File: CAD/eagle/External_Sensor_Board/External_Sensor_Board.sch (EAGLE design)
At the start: 12 parts, among them J1 SFW15R_FFC, U1 MAX31725MTA+, U2 HSCMNNN1.6BAAA3

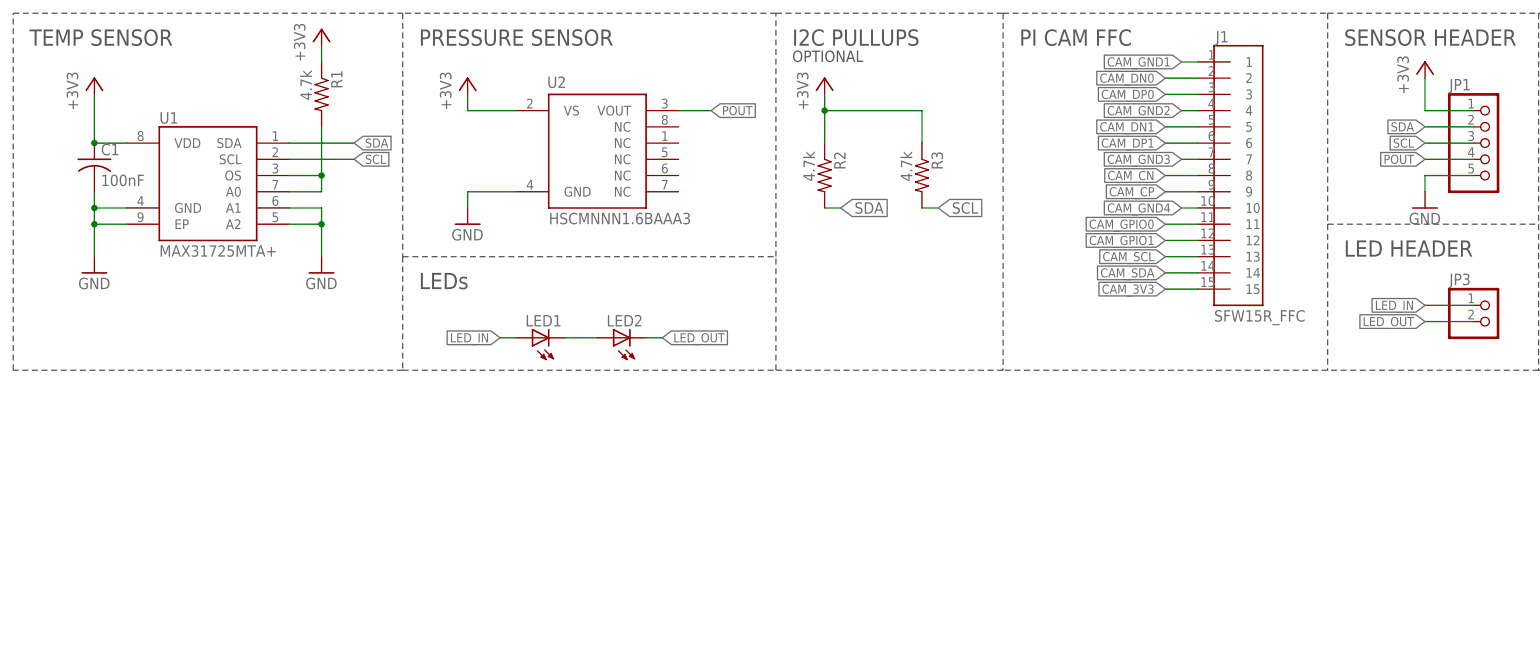
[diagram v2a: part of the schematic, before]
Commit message: Added I2C buffer to external sensor board.
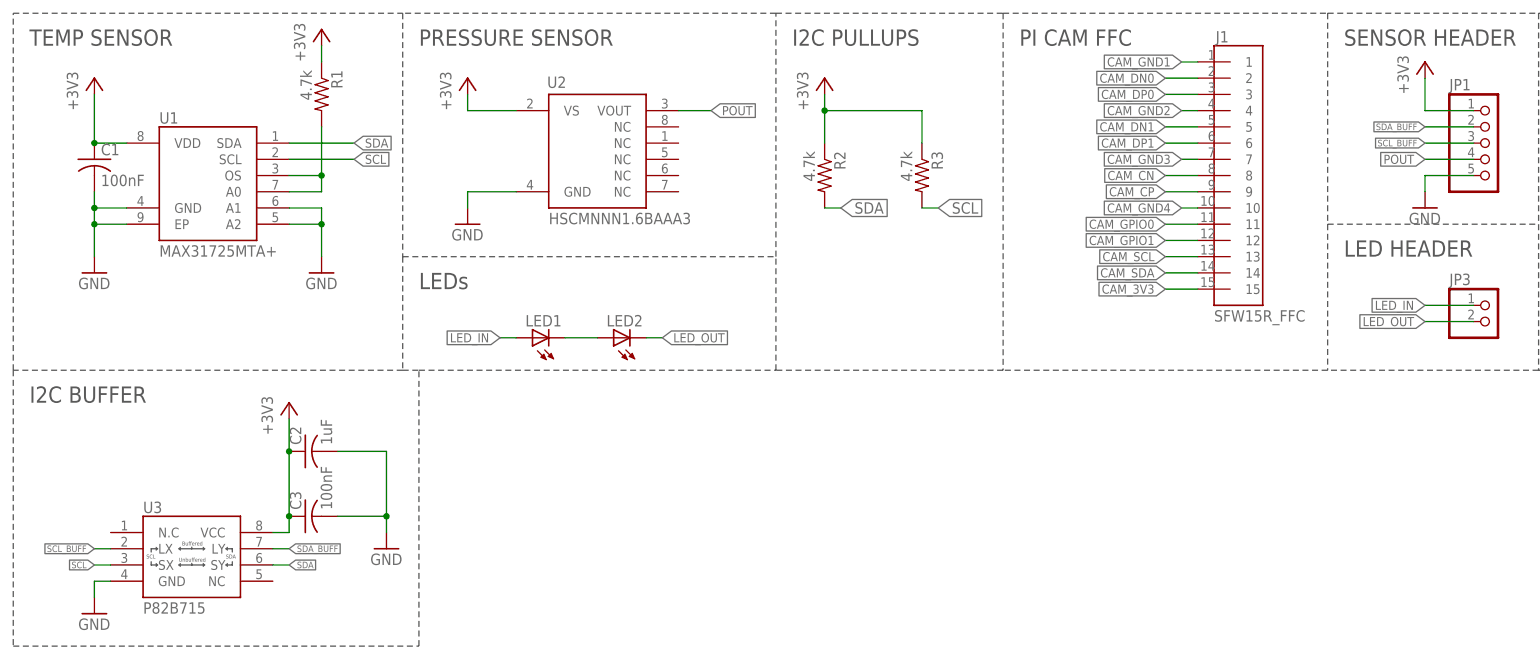
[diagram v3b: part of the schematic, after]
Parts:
- added C2: 1uF, resistor:C-USC0603
- added C3: 100nF, resistor:C-USC0603
- added U3: P82B715, CM_IC:P82B715
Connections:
- new net SCL_BUFF: JP1.3, U3.LX
- new net SDA_BUFF: JP1.2, U3.LY
- net +3V3: now also C2.1, C3.1, U3.VCC
- net GND: now also C2.2, C3.2, U3.GND
- net SCL: now also U3.SX; no longer JP1.3
- net SDA: now also U3.SY; no longer JP1.2
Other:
- note added: "I2C BUFFER"
- note removed: "OPTIONAL"
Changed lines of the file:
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@@
 <layer number="48" name="Document" color="7" fill="1" visible="no" active="no"/>
 <layer number="49" name="Reference" color="7" fill="1" visible="no" active="no"/>
+<layer number="50" name="dxf" color="7" fill="1" visible="no" active="no"/>
 <layer number="51" name="tDocu" color="7" fill="1" visible="no" active="no"/>
 <layer number="52" name="bDocu" color="7" fill="1" visible="no" active="no"/>
@@
 <layer number="98" name="Guide" color="6" fill="1" visible="yes" active="yes"/>
 <layer number="99" name="SpiceOrder" color="5" fill="1" visible="yes" active="yes"/>
+<layer number="100" name="Muster" color="7" fill="1" visible="no" active="no"/>
+<layer number="101" name="Patch_Top" color="12" fill="4" visible="yes" active="yes"/>
+<layer number="116" name="Patch_BOT" color="9" fill="4" visible="yes" active="yes"/>
+<layer number="200" name="200bmp" color="1" fill="10" visible="no" active="no"/>
+<layer number="250" name="Descript" color="3" fill="1" visible="yes" active="yes"/>
+<layer number="251" name="SMDround" color="12" fill="11" visible="no" active="no"/>
 </layers>
 <schematic xreflabel="%F%N/%S.%C%R" xrefpart="/%S.%C%R">
@@
 <part name="LED1" library="NR_LED" deviceset="LED_1206_NS" device=""/>
 <part name="LED2" library="NR_LED" deviceset="LED_1206_NS" device=""/>
+<part name="U3" library="CM_IC" deviceset="P82B715" device=""/>
+<part name="GND5" library="supply1" deviceset="GND" device=""/>
+<part name="+3V6" library="supply1" deviceset="+3V3" device=""/>
+<part name="C2" library="resistor" deviceset="C-US" device="C0603" value="1uF"/>
+<part name="C3" library="resistor" deviceset="C-US" device="C0603" value="100nF"/>
+<part name="GND6" library="supply1" deviceset="GND" device=""/>
 </parts>
 <sheets>
@@
 <wire x1="7.62" y1="152.4" x2="7.62" y2="208.28" width="0.1524" layer="97" style="shortdash"/>
 <text x="71.12" y="203.2" size="2.54" layer="97">PRESSURE SENSOR</text>
-<wire x1="68.58" y1="152.4" x2="127" y2="152.4" width="0.1524" layer="97" style="shortdash"/>
+<wire x1="68.58" y1="152.4" x2="71.12" y2="152.4" width="0.1524" layer="97" style="shortdash"/>
+<wire x1="71.12" y1="152.4" x2="127" y2="152.4" width="0.1524" layer="97" style="shortdash"/>
 <wire x1="127" y1="152.4" x2="127" y2="170.18" width="0.1524" layer="97" style="shortdash"/>
 <wire x1="127" y1="170.18" x2="127" y2="208.28" width="0.1524" layer="97" style="shortdash"/>
 <wire x1="127" y1="208.28" x2="68.58" y2="208.28" width="0.1524" layer="97" style="shortdash"/>
 <text x="129.54" y="203.2" size="2.54" layer="97">I2C PULLUPS</text>
-<text x="129.54" y="200.66" size="1.778" layer="97">OPTIONAL</text>
 <wire x1="127" y1="208.28" x2="162.56" y2="208.28" width="0.1524" layer="97" style="shortdash"/>
 <wire x1="162.56" y1="208.28" x2="162.56" y2="152.4" width="0.1524" layer="97" style="shortdash"/>
@@
 <text x="71.12" y="165.1" size="2.54" layer="97">LEDs</text>
 <wire x1="68.58" y1="170.18" x2="127" y2="170.18" width="0.1524" layer="97" style="shortdash"/>
+<text x="10.16" y="147.32" size="2.54" layer="97">I2C BUFFER</text>
+<wire x1="7.62" y1="152.4" x2="7.62" y2="109.22" width="0.1524" layer="97" style="shortdash"/>
+<wire x1="7.62" y1="109.22" x2="71.12" y2="109.22" width="0.1524" layer="97" style="shortdash"/>
+<wire x1="71.12" y1="109.22" x2="71.12" y2="152.4" width="0.1524" layer="97" style="shortdash"/>
 </plain>
 <instances>
@@
 <instance part="LED1" gate="G$1" x="91.44" y="157.48" rot="R90"/>
 <instance part="LED2" gate="G$1" x="104.14" y="157.48" rot="R90"/>
+<instance part="U3" gate="G$1" x="35.56" y="121.92"/>
+<instance part="GND5" gate="1" x="20.32" y="114.3"/>
+<instance part="+3V6" gate="G$1" x="50.8" y="147.32"/>
+<instance part="C2" gate="G$1" x="53.34" y="139.7" rot="R90"/>
+<instance part="C3" gate="G$1" x="53.34" y="129.54" rot="R90"/>
+<instance part="GND6" gate="1" x="66.04" y="124.46"/>
 </instances>
 <busses>
@@
 <wire x1="236.22" y1="193.04" x2="228.6" y2="193.04" width="0.1524" layer="91"/>
 <wire x1="228.6" y1="193.04" x2="228.6" y2="198.12" width="0.1524" layer="91"/>
+</segment>
+<segment>
+<pinref part="+3V6" gate="G$1" pin="+3V3"/>
+<pinref part="C2" gate="G$1" pin="1"/>
+<wire x1="50.8" y1="144.78" x2="50.8" y2="139.7" width="0.1524" layer="91"/>
+<pinref part="C3" gate="G$1" pin="1"/>
+<wire x1="50.8" y1="139.7" x2="50.8" y2="129.54" width="0.1524" layer="91"/>
+<junction x="50.8" y="139.7"/>
+<pinref part="U3" gate="G$1" pin="VCC"/>
+<wire x1="50.8" y1="129.54" x2="50.8" y2="127" width="0.1524" layer="91"/>
+<wire x1="50.8" y1="127" x2="48.26" y2="127" width="0.1524" layer="91"/>
+<junction x="50.8" y="129.54"/>
 </segment>
 </net>
@@
 <wire x1="228.6" y1="182.88" x2="228.6" y2="180.34" width="0.1524" layer="91"/>
 </segment>
+<segment>
+<pinref part="U3" gate="G$1" pin="GND"/>
+<pinref part="GND5" gate="1" pin="GND"/>
+<wire x1="22.86" y1="119.38" x2="20.32" y2="119.38" width="0.1524" layer="91"/>
+<wire x1="20.32" y1="119.38" x2="20.32" y2="116.84" width="0.1524" layer="91"/>
+</segment>
+<segment>
+<pinref part="C3" gate="G$1" pin="2"/>
+<pinref part="GND6" gate="1" pin="GND"/>
+<wire x1="58.42" y1="129.54" x2="66.04" y2="129.54" width="0.1524" layer="91"/>
+<wire x1="66.04" y1="129.54" x2="66.04" y2="127" width="0.1524" layer="91"/>
+<pinref part="C2" gate="G$1" pin="2"/>
+<wire x1="66.04" y1="129.54" x2="66.04" y2="139.7" width="0.1524" layer="91"/>
+<wire x1="66.04" y1="139.7" x2="58.42" y2="139.7" width="0.1524" layer="91"/>
+<junction x="66.04" y="129.54"/>
+</segment>
 </net>
 <net name="SDA" class="0">
@@
 </segment>
 <segment>
-<pinref part="JP1" gate="A" pin="2"/>
-<wire x1="236.22" y1="190.5" x2="228.6" y2="190.5" width="0.1524" layer="91"/>
-<label x="228.6" y="190.5" size="1.4224" layer="95" rot="R180" xref="yes"/>
+<pinref part="U3" gate="G$1" pin="SY"/>
+<wire x1="48.26" y1="121.92" x2="50.8" y2="121.92" width="0.1524" layer="91"/>
+<label x="50.8" y="121.92" size="1.016" layer="95" xref="yes"/>
 </segment>
 </net>
@@
 </segment>
 <segment>
-<pinref part="JP1" gate="A" pin="3"/>
-<wire x1="236.22" y1="187.96" x2="228.6" y2="187.96" width="0.1524" layer="91"/>
-<label x="228.6" y="187.96" size="1.4224" layer="95" rot="R180" xref="yes"/>
+<pinref part="U3" gate="G$1" pin="SX"/>
+<wire x1="22.86" y1="121.92" x2="20.32" y2="121.92" width="0.1524" layer="91"/>
+<label x="20.32" y="121.92" size="1.016" layer="95" rot="R180" xref="yes"/>
 </segment>
 </net>
@@
 </segment>
 </net>
+<net name="SDA_BUFF" class="0">
+<segment>
+<pinref part="U3" gate="G$1" pin="LY"/>
+<wire x1="48.26" y1="124.46" x2="50.8" y2="124.46" width="0.1524" layer="91"/>
+<label x="50.8" y="124.46" size="1.016" layer="95" xref="yes"/>
+</segment>
+<segment>
+<pinref part="JP1" gate="A" pin="2"/>
+<wire x1="236.22" y1="190.5" x2="228.6" y2="190.5" width="0.1524" layer="91"/>
+<label x="228.6" y="190.5" size="1.016" layer="95" rot="R180" xref="yes"/>
+</segment>
+</net>
+<net name="SCL_BUFF" class="0">
+<segment>
+<pinref part="U3" gate="G$1" pin="LX"/>
+<wire x1="22.86" y1="124.46" x2="20.32" y2="124.46" width="0.1524" layer="91"/>
+<label x="20.32" y="124.46" size="1.016" layer="95" rot="R180" xref="yes"/>
+</segment>
+<segment>
+<pinref part="JP1" gate="A" pin="3"/>
+<wire x1="236.22" y1="187.96" x2="228.6" y2="187.96" width="0.1524" layer="91"/>
+<label x="228.6" y="187.96" size="1.016" layer="95" rot="R180" xref="yes"/>
+</segment>
+</net>

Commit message: Altered external sensor board to use J30J-25 connector instead of headers. Board is final aside from logos.
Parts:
- removed JP1: (no value), pinhead:PINHD-1X5
- removed JP2: (no value), pinhead:PINHD-1X15
- removed JP3: (no value), pinhead:PINHD-1X2
- added J2: J30J-25, CM_J30J:J30J-25
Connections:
- removed net CAM_CN: J1.8, JP2.8
- removed net CAM_CP: J1.9, JP2.9
- removed net CAM_DN0: J1.2, JP2.2
- removed net CAM_DN1: J1.5, JP2.5
- removed net CAM_DP0: J1.3, JP2.3
- removed net CAM_DP1: J1.6, JP2.6
- new net CAM_C_N: J1.8, J2.10
- new net CAM_C_P: J1.9, J2.12
- new net CAM_D0_N: J1.2, J2.2
- new net CAM_D0_P: J1.3, J2.4
- new net CAM_D1_N: J1.5, J2.6
- new net CAM_D1_P: J1.6, J2.8
- net +3V3: now also J2.19; no longer JP1.1
- net CAM_3V3: now also J2.22; no longer JP2.15
- net CAM_GND1: now also J2.1; no longer JP2.1
- net CAM_GND2: now also J2.3; no longer JP2.4
- net CAM_GND3: now also J2.5; no longer JP2.7
- net CAM_GND4: now also J2.7; no longer JP2.10
- net CAM_GPIO0: now also J2.9; no longer JP2.11
- net CAM_GPIO1: now also J2.11; no longer JP2.12
- net CAM_SCL: now also J2.13; no longer JP2.13
- net CAM_SDA: now also J2.20; no longer JP2.14
- net GND: now also J2.15; no longer JP1.5
- net LED_IN: now also J2.14; no longer JP3.1
- net LED_OUT: now also J2.24; no longer JP3.2
- net POUT: now also J2.17; no longer JP1.4
- net SCL_BUFF: now also J2.25; no longer JP1.3
- net SDA_BUFF: now also J2.23; no longer JP1.2
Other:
- note added: "EXTERNAL BOARD MDM"
- note removed: "CAM HEADER"
- note removed: "LED HEADER"
- note removed: "SENSOR HEADER"

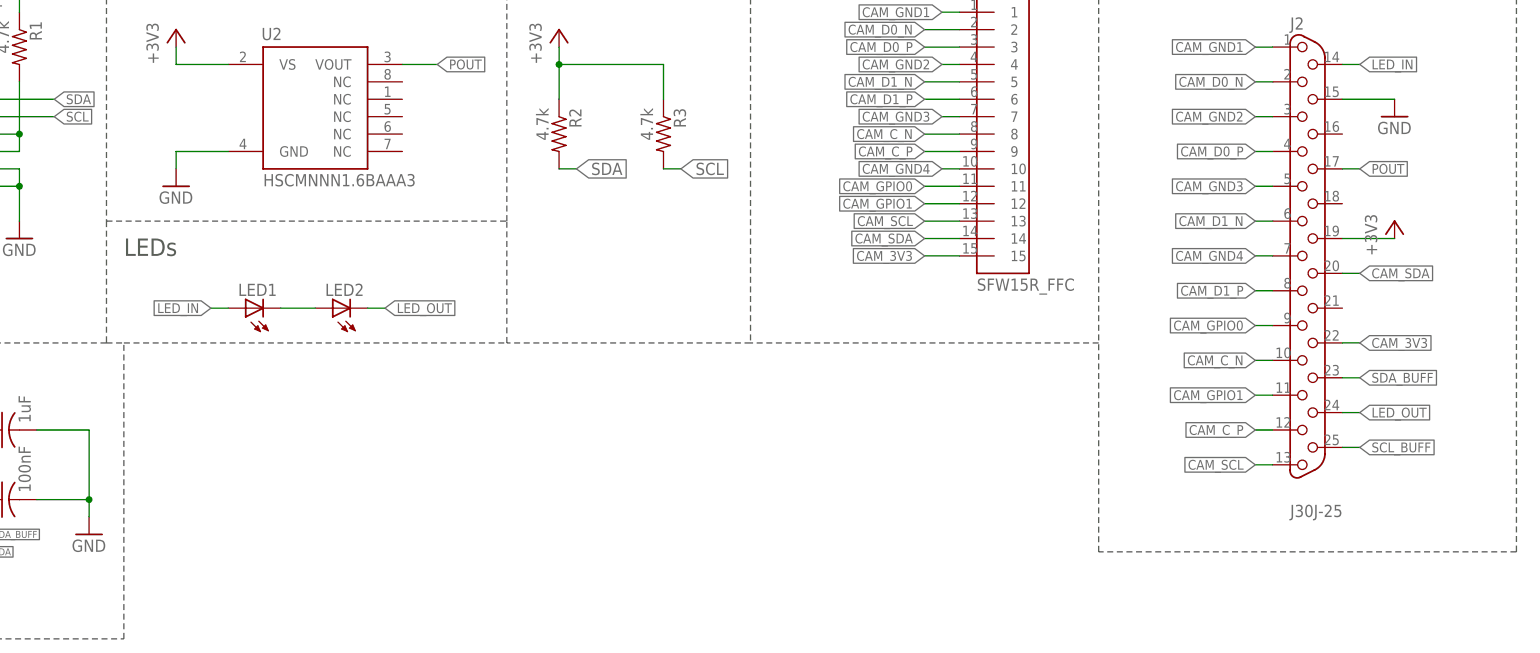
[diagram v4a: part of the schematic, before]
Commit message: Added bias voltage route to external board
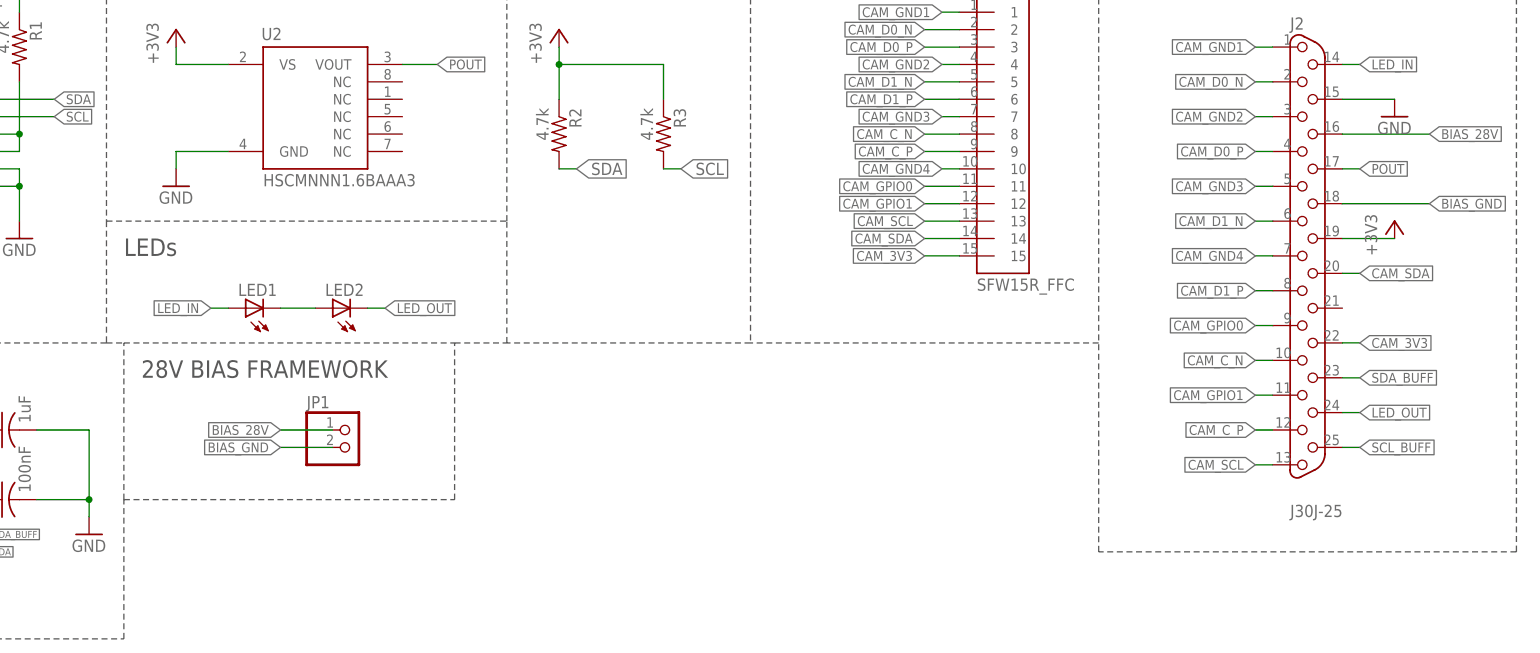
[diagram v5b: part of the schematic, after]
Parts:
- added JP1: (no value), pinhead:PINHD-1X2
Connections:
- new net BIAS_28V: J2.16, JP1.1
- new net BIAS_GND: J2.18, JP1.2
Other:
- note added: "28V BIAS FRAMEWORK"
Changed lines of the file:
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@@
 <part name="+3V7" library="supply1" deviceset="+3V3" device=""/>
 <part name="GND7" library="supply1" deviceset="GND" device=""/>
+<part name="JP1" library="pinhead" deviceset="PINHD-1X2" device=""/>
 </parts>
 <sheets>
@@
 <text x="71.12" y="203.2" size="2.54" layer="97">PRESSURE SENSOR</text>
 <wire x1="68.58" y1="152.4" x2="71.12" y2="152.4" width="0.1524" layer="97" style="shortdash"/>
-<wire x1="71.12" y1="152.4" x2="127" y2="152.4" width="0.1524" layer="97" style="shortdash"/>
+<wire x1="71.12" y1="152.4" x2="119.38" y2="152.4" width="0.1524" layer="97" style="shortdash"/>
+<wire x1="119.38" y1="152.4" x2="127" y2="152.4" width="0.1524" layer="97" style="shortdash"/>
 <wire x1="127" y1="152.4" x2="127" y2="170.18" width="0.1524" layer="97" style="shortdash"/>
 <wire x1="127" y1="170.18" x2="127" y2="208.28" width="0.1524" layer="97" style="shortdash"/>
@@
 <wire x1="7.62" y1="152.4" x2="7.62" y2="109.22" width="0.1524" layer="97" style="shortdash"/>
 <wire x1="7.62" y1="109.22" x2="71.12" y2="109.22" width="0.1524" layer="97" style="shortdash"/>
-<wire x1="71.12" y1="109.22" x2="71.12" y2="152.4" width="0.1524" layer="97" style="shortdash"/>
+<wire x1="71.12" y1="109.22" x2="71.12" y2="129.54" width="0.1524" layer="97" style="shortdash"/>
+<wire x1="71.12" y1="129.54" x2="71.12" y2="152.4" width="0.1524" layer="97" style="shortdash"/>
 <wire x1="274.32" y1="121.92" x2="213.36" y2="121.92" width="0.1524" layer="97" style="shortdash"/>
 <wire x1="213.36" y1="121.92" x2="213.36" y2="152.4" width="0.1524" layer="97" style="shortdash"/>
+<text x="73.66" y="147.32" size="2.54" layer="97">28V BIAS FRAMEWORK</text>
+<wire x1="71.12" y1="129.54" x2="119.38" y2="129.54" width="0.1524" layer="97" style="shortdash"/>
+<wire x1="119.38" y1="129.54" x2="119.38" y2="152.4" width="0.1524" layer="97" style="shortdash"/>
 </plain>
 <instances>
@@
 <instance part="+3V7" gate="G$1" x="256.54" y="170.18"/>
 <instance part="GND7" gate="1" x="256.54" y="185.42"/>
+<instance part="JP1" gate="G$1" x="104.14" y="137.16"/>
 </instances>
 <busses>
@@
 </segment>
 </net>
+<net name="BIAS_28V" class="0">
+<segment>
+<pinref part="JP1" gate="G$1" pin="1"/>
+<wire x1="101.6" y1="139.7" x2="93.98" y2="139.7" width="0.1524" layer="91"/>
+<label x="93.98" y="139.7" size="1.4224" layer="95" rot="R180" xref="yes"/>
+</segment>
+<segment>
+<pinref part="J2" gate="G$1" pin="16"/>
+<wire x1="248.92" y1="182.88" x2="261.62" y2="182.88" width="0.1524" layer="91"/>
+<label x="261.62" y="182.88" size="1.4224" layer="95" xref="yes"/>
+</segment>
+</net>
+<net name="BIAS_GND" class="0">
+<segment>
+<pinref part="JP1" gate="G$1" pin="2"/>
+<wire x1="101.6" y1="137.16" x2="93.98" y2="137.16" width="0.1524" layer="91"/>
+<label x="93.98" y="137.16" size="1.4224" layer="95" rot="R180" xref="yes"/>
+</segment>
+<segment>
+<pinref part="J2" gate="G$1" pin="18"/>
+<wire x1="248.92" y1="172.72" x2="261.62" y2="172.72" width="0.1524" layer="91"/>
+<label x="261.62" y="172.72" size="1.4224" layer="95" xref="yes"/>
+</segment>
+</net>
